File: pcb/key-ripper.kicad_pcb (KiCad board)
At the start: 2 copper layers, 285.8 x 116.7 mm, 193 parts, among them J1 Conn_01x03, SW1 ESC, SW10 F9, SW11 F10, SW12 F11, SW13 F12, SW14 TILDE, SW15 1, SW16 2, SW17 3, SW18 4, SW19 5, SW2 F1, SW20 6, SW21 7, SW22 8, SW23 9, SW24 0, SW25 -, SW26 +, SW27 BACKSPACE, SW28 TAB, SW29 Q, SW3 F2, SW30 W, SW31 E, SW32 R, SW33 T, SW34 Y, SW35 U, SW36 I, SW37 O, SW38 P, SW39 [, SW4 F3, SW40 ], SW41 BACKSLASH, SW42 CAPS, SW43 A, SW44 S, SW45 D, SW46 F, SW47 G, SW48 H, SW49 J, SW5 F4, SW50 K, SW51 L, SW52 ;, SW53 ', SW54 ENTER, SW55 L_SHIFT, SW56 Z, SW57 X, SW58 C, SW59 V, SW6 F5, SW60 B, SW61 N, SW62 M, SW63 ,, SW64 ., SW65 FWD_SLASH, SW66 UP, SW67 FN, SW68 BL_CTRL, SW69 L_ALT, SW7 F6, SW70 L_CMD, SW71 SPACE, SW72 R_CMD, SW73 LEFT, SW74 DOWN, SW75 RIGHT, SW8 F7, SW9 F8, U1 RP2040, U2 TYPE-C-31-M-12, U3 XC6206PxxxMR, U4 W25Q128JVS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

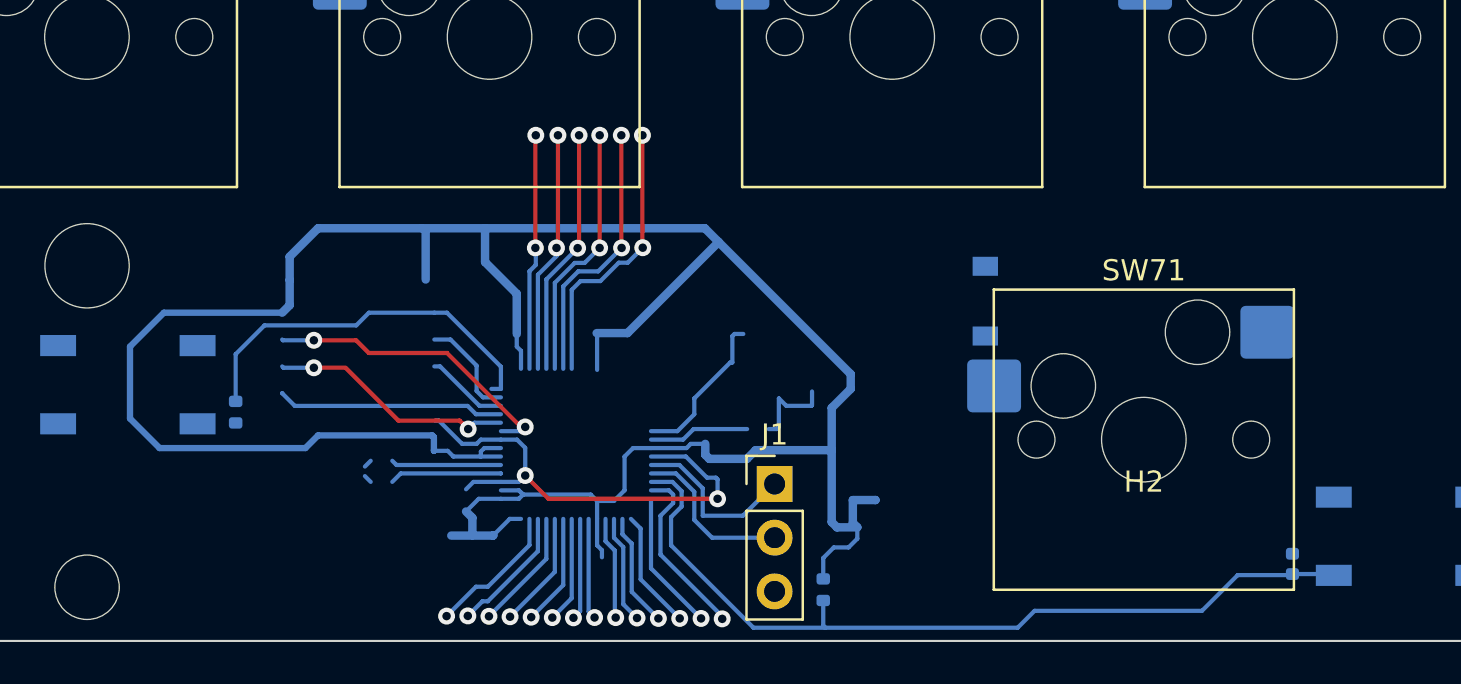
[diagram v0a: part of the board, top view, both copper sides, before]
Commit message: Clean up stray wires
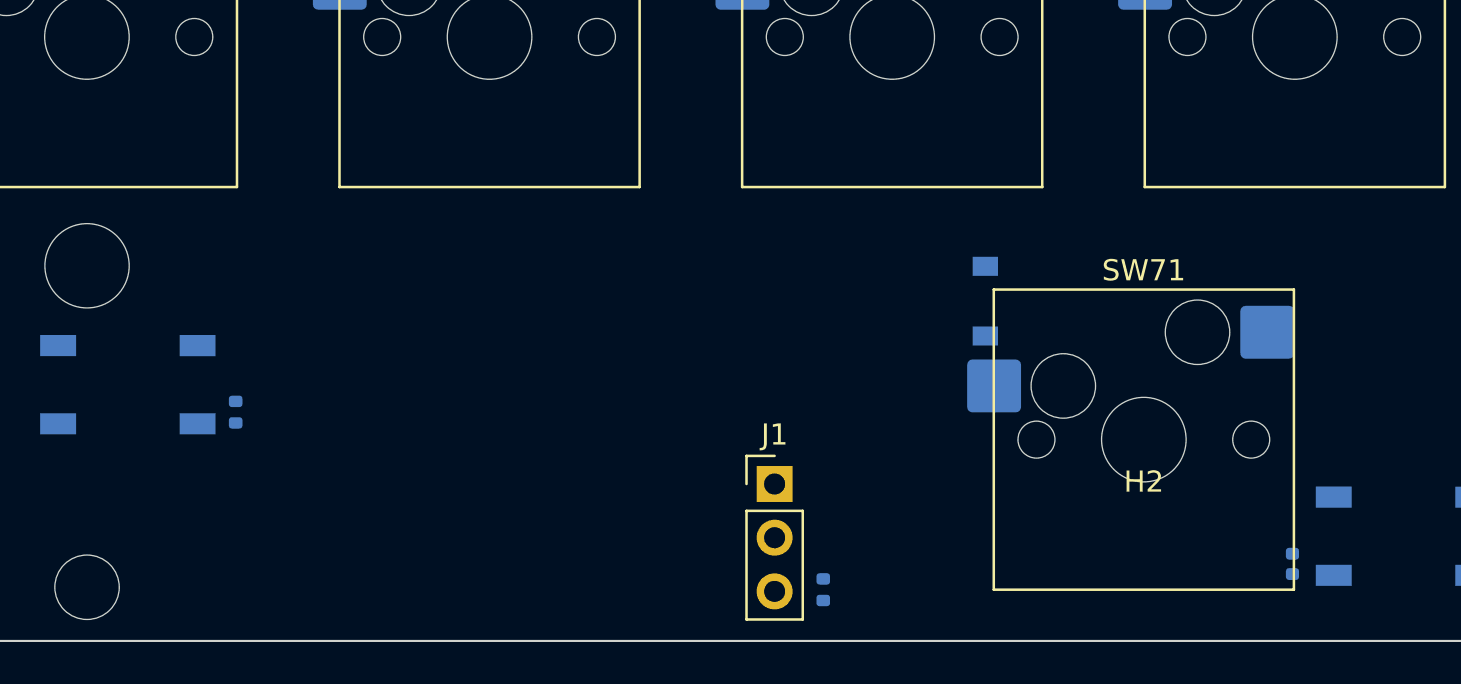
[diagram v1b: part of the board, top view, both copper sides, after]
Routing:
- net +3V3: track 127.5 -> 0.00 mm
- net RUN: track 39.8 -> 0.16 mm
- net +1V1: track 23.4 -> 0.00 mm, vias 2 -> 0
- net QSPI_SS: track 26.6 -> 8.44 mm
- net QSPI_SD3: track 36.1 -> 21.7 mm, vias 2 -> 0
- net ROW5: track 13.2 -> 0.00 mm, vias 2 -> 0
- net ROW4: track 12.7 -> 0.00 mm, vias 2 -> 0
- net ROW3: track 12.2 -> 0.00 mm, vias 2 -> 0
- net QSPI_SCLK: track 30.7 -> 19.0 mm, vias 2 -> 0
- net ROW2: track 11.7 -> 0.00 mm, vias 2 -> 0
- net ROW1: track 11.4 -> 0.00 mm, vias 2 -> 0
- net ROW0: track 11.2 -> 0.00 mm, vias 2 -> 0
- net QSPI_SD0: track 25.6 -> 14.9 mm
- net CLM13: track 8.47 -> 0.00 mm, vias 1 -> 0
- net SWCLK: track 8.22 -> 0.00 mm
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
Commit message: Connect the columns together
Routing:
- net ROW0: track 0.00 -> 266.7 mm
- net CLM1: track 0.00 -> 132.5 mm, vias 0 -> 2
- net CLM11: track 0.00 -> 126.7 mm
- net CLM12: track 0.00 -> 126.5 mm
- net CLM10: track 0.00 -> 123.4 mm
- net CLM2: track 0.00 -> 122.8 mm
- net CLM3: track 0.00 -> 120.5 mm
- net CLM5: track 0.00 -> 110.6 mm
- net CLM13: track 0.00 -> 103.2 mm
- net CLM8: track 0.00 -> 100.6 mm
- net CLM9: track 0.00 -> 99.4 mm
- net CLM4: track 0.00 -> 99.1 mm
- net CLM0: track 0.00 -> 98.1 mm
- net CLM7: track 0.00 -> 94.5 mm
- net CLM6: track 0.00 -> 91.8 mm

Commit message: Connect the rows together
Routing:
- net ROW5: track 0.00 -> 326.0 mm, vias 0 -> 9
- net ROW2: track 0.00 -> 271.3 mm, vias 0 -> 13
- net ROW1: track 0.00 -> 269.5 mm, vias 0 -> 13
- net ROW3: track 0.00 -> 255.7 mm, vias 0 -> 12
- net ROW4: track 0.00 -> 238.1 mm, vias 0 -> 11

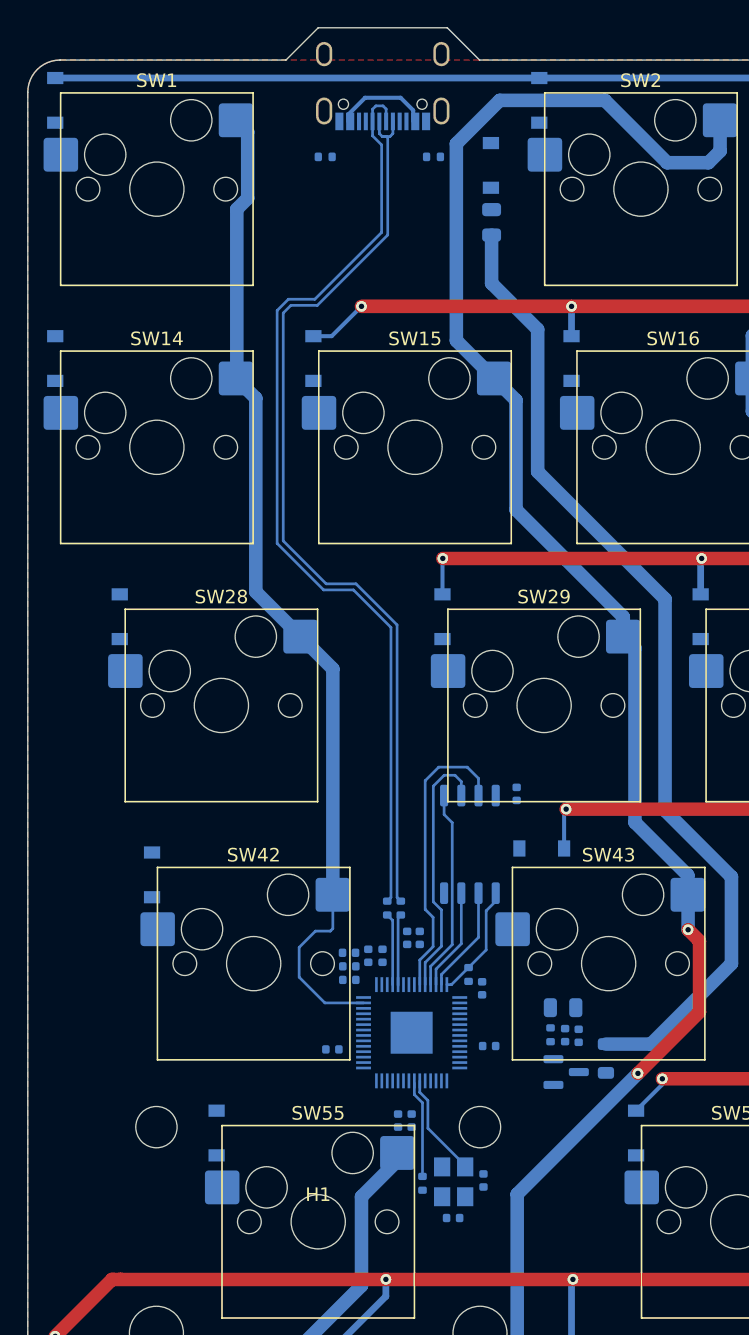
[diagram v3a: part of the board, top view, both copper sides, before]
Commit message: Connect rows across the ground plane
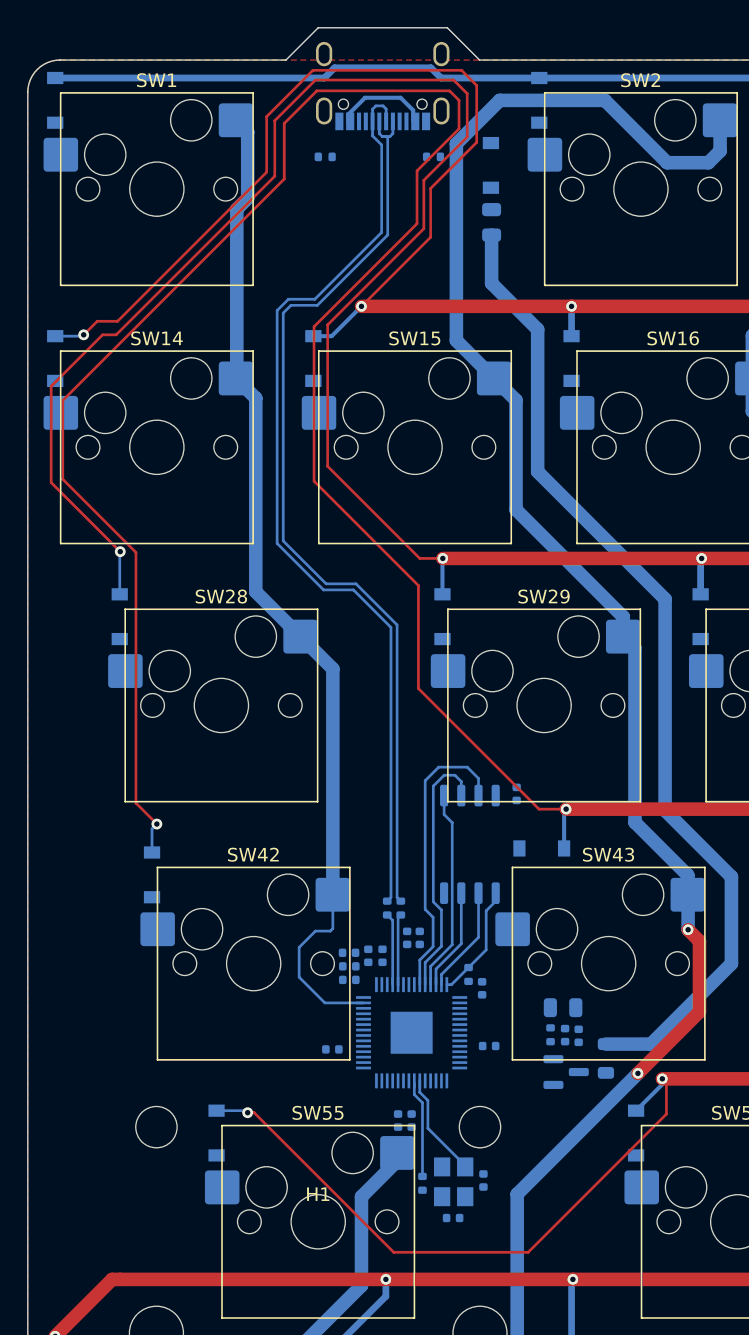
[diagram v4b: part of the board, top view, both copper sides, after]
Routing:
- net ROW3: track 255.7 -> 399.1 mm, vias 12 -> 13
- net ROW2: track 271.3 -> 374.8 mm, vias 13 -> 14
- net ROW1: track 269.5 -> 331.5 mm, vias 13 -> 14
- net ROW4: track 238.1 -> 282.6 mm, vias 11 -> 12
- net ROW0: track 266.7 -> 267.3 mm

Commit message: Starting more simplifications
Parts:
- moved F1 1.56 mm to (23.1, -16.8)
- moved D76 1.56 mm to (23.1, -20.9)
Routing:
- net ROW3: track 399.1 -> 38.6 mm, vias 13 -> 12
- net ROW2: track 374.8 -> 35.7 mm, vias 14 -> 13
- net ROW1: track 331.5 -> 35.1 mm, vias 14 -> 13
- net ROW5: track 326.0 -> 57.5 mm
- net ROW4: track 282.6 -> 32.4 mm, vias 12 -> 10
- net CLM0: track 98.1 -> 84.8 mm
- net CLM1: track 132.5 -> 122.4 mm, vias 2 -> 0
- net Net-(F1-Pad2): track 72.8 -> 71.1 mm

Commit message: Route rows more consistently
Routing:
- net ROW1: track 35.1 -> 260.7 mm, vias 13 -> 5
- net ROW2: track 35.7 -> 259.1 mm, vias 13 -> 2
- net ROW5: track 57.5 -> 272.9 mm, vias 9 -> 2
- net ROW3: track 38.6 -> 251.0 mm, vias 12 -> 2
- net ROW4: track 32.4 -> 238.5 mm, vias 10 -> 2
- net ROW0: track 267.3 -> 268.5 mm, vias 0 -> 2

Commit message: Resize the column connectors
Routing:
- net CLM4: track 99.1 -> 103.6 mm
- net CLM3: track 120.5 -> 125.0 mm
- net CLM12: track 126.5 -> 130.4 mm
- net CLM11: track 126.7 -> 129.2 mm
- net USB-: track 70.0 -> 67.6 mm
- net USB+: track 68.7 -> 66.3 mm
- net CLM2: track 122.8 -> 124.9 mm
- net CLM6: track 91.8 -> 93.9 mm
- net CLM5: track 110.6 -> 112.5 mm
- net CLM10: track 123.4 -> 125.2 mm
- net CLM7: track 94.5 -> 95.2 mm

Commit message: Connect the key switches to their respective diodes
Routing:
- net Net-(D43-Pad2): track 0.00 -> 6.17 mm
- net Net-(D75-Pad2): track 0.00 -> 2.53 mm
- net Net-(D39-Pad2): track 0.00 -> 2.53 mm
- net Net-(D23-Pad2): track 0.00 -> 2.53 mm
- net Net-(D64-Pad2): track 0.00 -> 2.53 mm
- net Net-(D54-Pad2): track 0.00 -> 2.53 mm
- net Net-(D49-Pad2): track 0.00 -> 2.53 mm
- net Net-(D13-Pad2): track 0.00 -> 2.53 mm
- net Net-(D71-Pad2): track 0.00 -> 2.53 mm
- net Net-(D32-Pad2): track 0.00 -> 2.53 mm
- net Net-(D31-Pad2): track 0.00 -> 2.53 mm
- net Net-(D21-Pad2): track 0.00 -> 2.53 mm
- net Net-(D20-Pad2): track 0.00 -> 2.53 mm
- net Net-(D19-Pad2): track 0.00 -> 2.53 mm
- net Net-(D60-Pad2): track 0.00 -> 2.53 mm
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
